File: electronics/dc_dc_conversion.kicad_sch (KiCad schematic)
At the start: 10 parts, among them U1 AZ1117-ADJ, U2 AZ1117-ADJ

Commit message: no tracks, but placement looks good
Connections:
- net GND: no longer C1.2, C2.1, R2.2
- net GND_LP: now reaches R4.2
- net GND_LP: now also C1.2, C2.1, R2.2

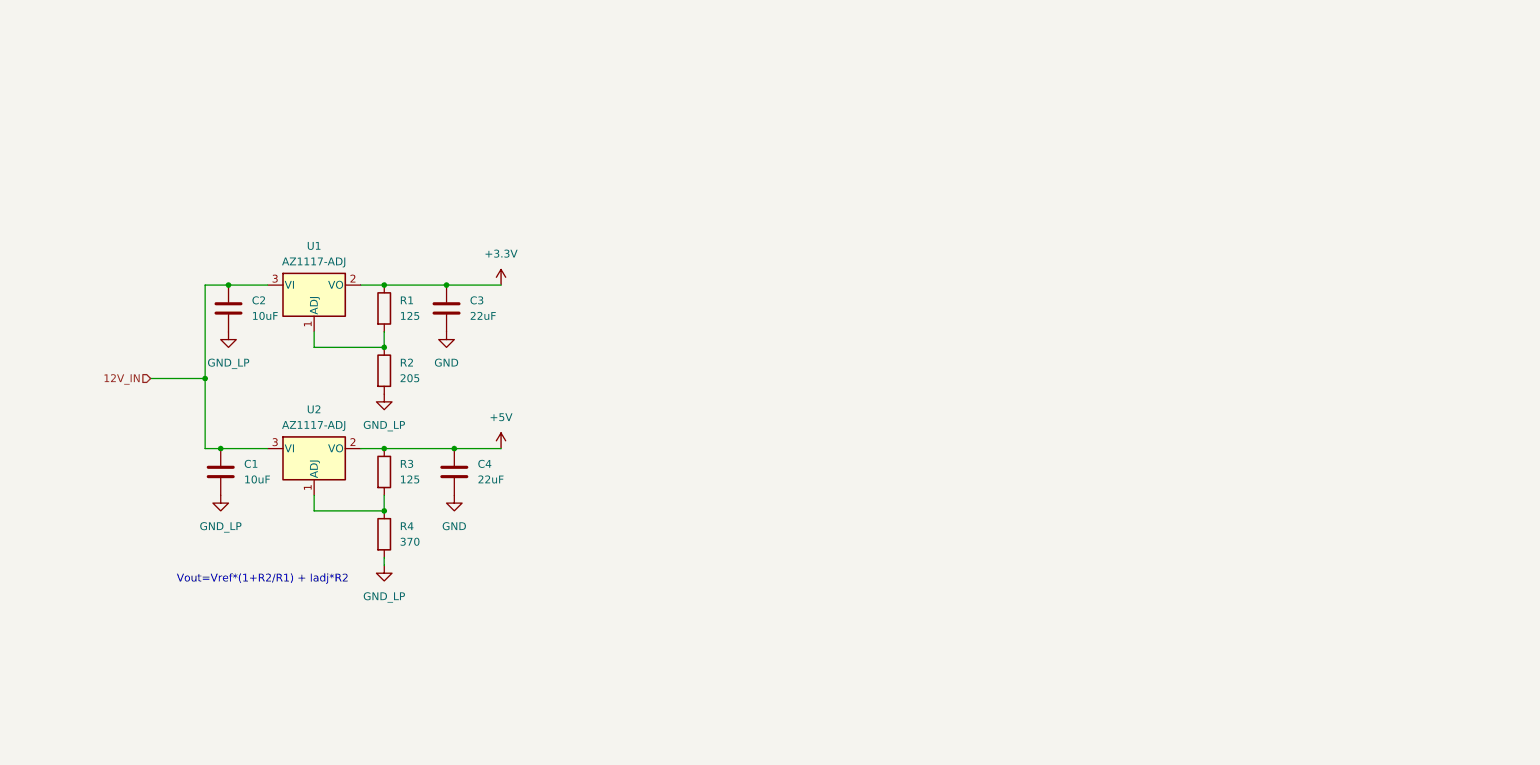
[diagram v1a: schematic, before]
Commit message: add some more part nummbers
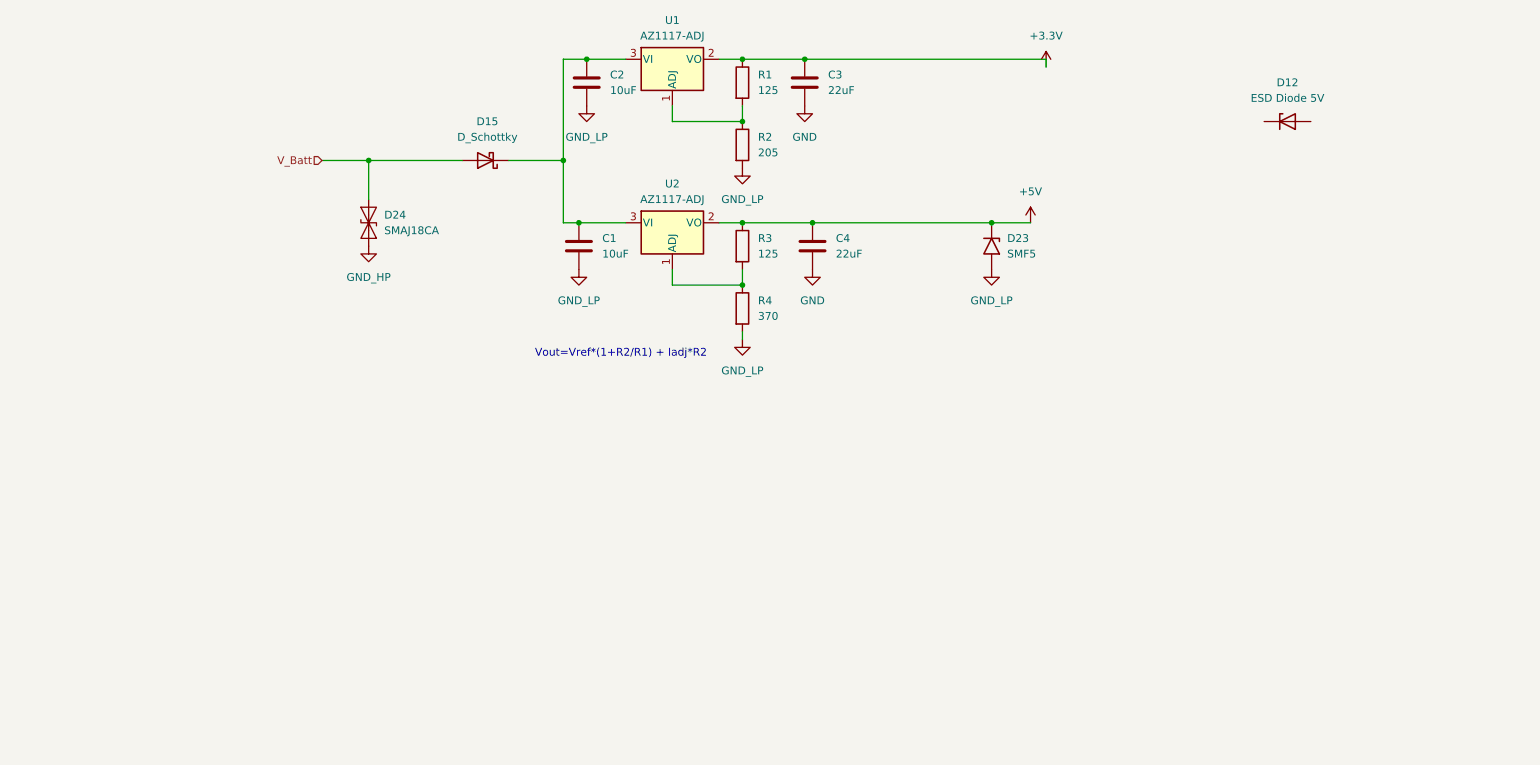
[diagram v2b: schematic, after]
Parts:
- added D12: ESD Diode 5V, Diode_SMD:Nexperia_DSN1608-2_1.6x0.8mm, symbol Diode:PTVS5V0Z1USK
- added D15: D_Schottky, Diode_SMD:D_SMB, symbol Device:D_Schottky
- added D23: SMF5, Diode_SMD:D_SMF, symbol Diode:SMF7V0A
- added D24: SMAJ18CA, Diode_SMD:D_SMA, symbol Diode:SMAJ18CA
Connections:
- net +5V: now also D23.1 (A1)
- net GND_LP: now also D23.2 (A2)
- net 12V_IN: no longer names the net of C1.1, C2.2, U1.3 (VI), U2.3 (VI)
- net 12V_IN: now also D15.1 (K)
- new net GND_HP: D24.1 (A1)
- new net V_Batt: D15.2 (A), D24.2 (A2)
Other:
- moved on the sheet: C1, C2, C3, C4, R1, R2, R3, R4, U1, U2

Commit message: capacitors added. universal dc/dc converters
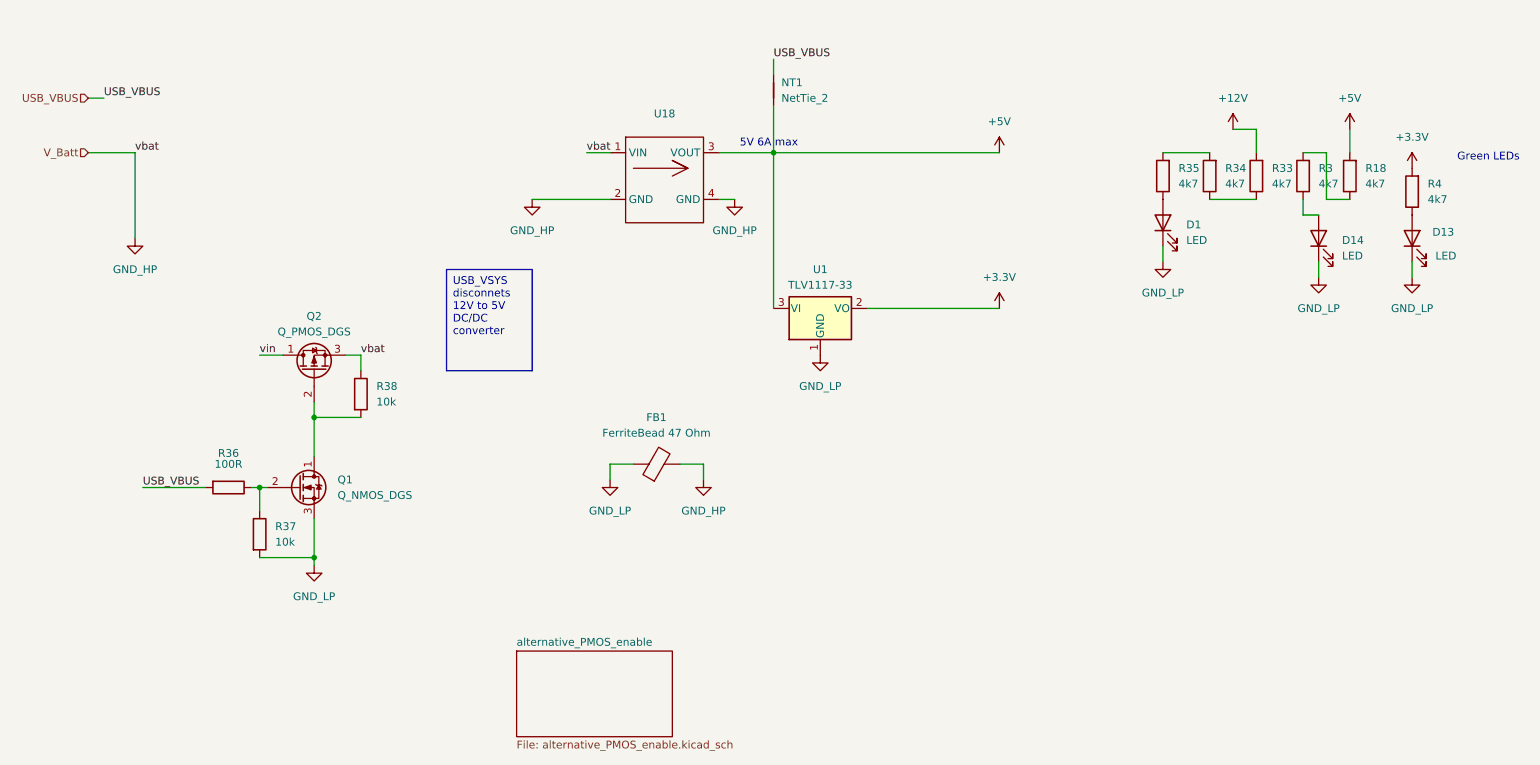
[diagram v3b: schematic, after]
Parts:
- removed C1, C2: 10uF, Capacitor_SMD:C_0805_2012Metric_Pad1.18x1.45mm_HandSolder, symbol Device:C
- removed C3, C4: 22uF, Capacitor_SMD:C_0805_2012Metric_Pad1.18x1.45mm_HandSolder, symbol Device:C
- removed D12: ESD Diode 5V, Diode_SMD:Nexperia_DSN1608-2_1.6x0.8mm, symbol Diode:PTVS5V0Z1USK
- removed D15: D_Schottky, Diode_SMD:D_SMB, symbol Device:D_Schottky
- removed D23: SMF5, Diode_SMD:D_SMF, symbol Diode:SMF7V0A
- removed D24: SMAJ18CA, Diode_SMD:D_SMA, symbol Diode:SMAJ18CA
- removed R1: 125, Resistor_SMD:R_0805_2012Metric_Pad1.20x1.40mm_HandSolder, symbol Device:R
- removed R2: 205, Resistor_SMD:R_0805_2012Metric_Pad1.20x1.40mm_HandSolder, symbol Device:R
- removed U1, U2: AZ1117-ADJ, Package_TO_SOT_SMD:SOT-223-3_TabPin2, symbol Regulator_Linear:AZ1117-ADJ
- added D1, D13, D14: LED, LED_SMD:LED_1206_3216Metric, symbol Device:LED
- added FB1: FerriteBead 47 Ohm, Inductor_SMD:L_Walsin_WLFM201609x, symbol Device:FerriteBead
- added NT1: NetTie_2, NetTie:NetTie-2_THT_Pad1.0mm, symbol Device:NetTie_2
- added Q1: Q_NMOS_DGS, Package_TO_SOT_SMD:SOT-323_SC-70, symbol Device:Q_NMOS_DGS
- added Q2: Q_PMOS_DGS, Package_TO_SOT_SMD:SOT-323_SC-70, symbol Device:Q_PMOS_DGS
- added R18, R33, R34, R35: 4k7, Resistor_SMD:R_0805_2012Metric, symbol Device:R
- added R36: 100R, Resistor_SMD:R_0805_2012Metric, symbol Device:R
- added R37, R38: 10k, Resistor_SMD:R_0805_2012Metric, symbol Device:R
- added U1: TLV1117-33, Package_TO_SOT_SMD:SOT-223-3_TabPin2, symbol Regulator_Linear:TLV1117-33
- added U18: ~, HeavyDuty:mini360, symbol HeavyDuty:DC/DC_Buck_Converter
- R3: value 125 -> 4k7; footprint Resistor_SMD:R_0805_2012Metric_Pad1.20x1.40mm_HandSolder -> Resistor_SMD:R_0805_2012Metric
- R4: value 370 -> 4k7; footprint Resistor_SMD:R_0805_2012Metric_Pad1.20x1.40mm_HandSolder -> Resistor_SMD:R_0805_2012Metric
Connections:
- net +3.3V: now also R4.2, U1.2 (VO)
- net +5V: now also NT1.1, R18.2, U1.3 (VI), U18.3 (VOUT); no longer R3.1
- net GND_HP: now also FB1.2, Q2.3 (S), R38.1, U18.1 (VIN), U18.2 (GND), U18.4 (GND)
- net GND_LP: now also D1.1 (K), D13.1 (K), D14.1 (K), FB1.1, Q1.3 (S), R37.2, U1.1 (GND); no longer R4.2
- net at R3.2: now also R18.1; no longer R4.1
- new net: D14.2 (A), R3.1
- new net: R33.1, R34.1
- new net: D13.2 (A), R4.1
- new net: D1.2 (A), R35.1
- new net: R34.2, R35.2
- new net: Q1.1 (D), Q2.2 (G), R38.2
- new net: Q1.2 (G), R36.1, R37.1
- new net +12V: R33.2
- new net USB_VBUS: NT1.2, R36.2
- new net vin: Q2.1 (D)
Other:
- added sheet alternative_PMOS_enable (alternative_PMOS_enable.kicad_sch)
- note added: "5V 6A max"
- note added: "Green LEDs"
- note removed: "Vout=Vref*(1+R2/R1) + Iadj*R2"
